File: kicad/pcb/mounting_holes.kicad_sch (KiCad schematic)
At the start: 34 parts

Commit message: schematic fix and plate tolerance fix
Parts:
- removed H11, H13, H14, H15, H16, H17, H18, H19, H20, H21, H22, H23, H24, H25, H26, H27, H28, H30, H31, H32, H33, H34, H35, H36, H37, H38: M2 Hole, MountingHole:MountingHole_2.2mm_M2_DIN965, symbol Mechanical:MountingHole
- added H1 (x4), H2 (x4), H3 (x3), H4 (x3), H5 (x3), H6 (x2), H7 (x2), H8 (x2): M2 Hole, capacitive_sensors:MountingHole_2.2mm_M2, symbol Mechanical:MountingHole
- added H6, H7, H8: M2 Hole, MountingHole:MountingHole_2.2mm_M2, symbol Mechanical:MountingHole
- H1, H2, H3, H4, H5, H6, H7: footprint MountingHole:MountingHole_2.2mm_M2_DIN965 -> capacitive_sensors:MountingHole_2.2mm_M2
- H8: footprint MountingHole:MountingHole_2.2mm_M2_DIN965 -> MountingHole:MountingHole_2.2mm_M2
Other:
- moved on the sheet: H1, H2, H3, H4, H5, H6, H7, H8

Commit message: remove top mounting hole for chiffre+ compatibility
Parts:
- H5: now not fitted
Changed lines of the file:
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@@
   )
   (symbol (lib_id "Mechanical:MountingHole") (at 50.8 55.88 0) (unit 1)
-    (in_bom yes) (on_board yes) (dnp no) (fields_autoplaced)
+    (in_bom yes) (on_board yes) (dnp yes) (fields_autoplaced)
     (property "Reference" "H5" (at 53.34 54.61 0)
       (effects (font (size 1.27 1.27)) (justify left))
@@
   )
   (symbol (lib_id "Mechanical:MountingHole") (at 50.8 71.12 0) (unit 1)
-    (in_bom yes) (on_board yes) (dnp no) (fields_autoplaced)
+    (in_bom yes) (on_board yes) (dnp yes) (fields_autoplaced)
     (property "Reference" "H5" (at 53.34 69.85 0)
       (effects (font (size 1.27 1.27)) (justify left))

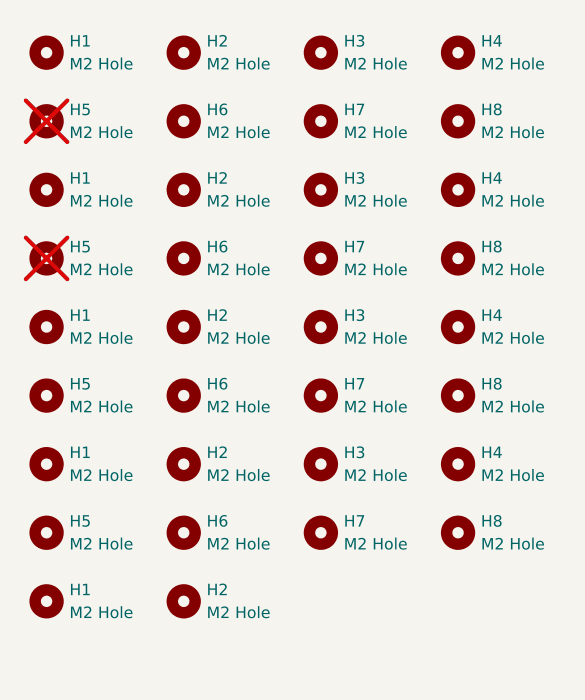
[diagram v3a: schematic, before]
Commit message: Remove extra mounting holes from PCB and update version number.
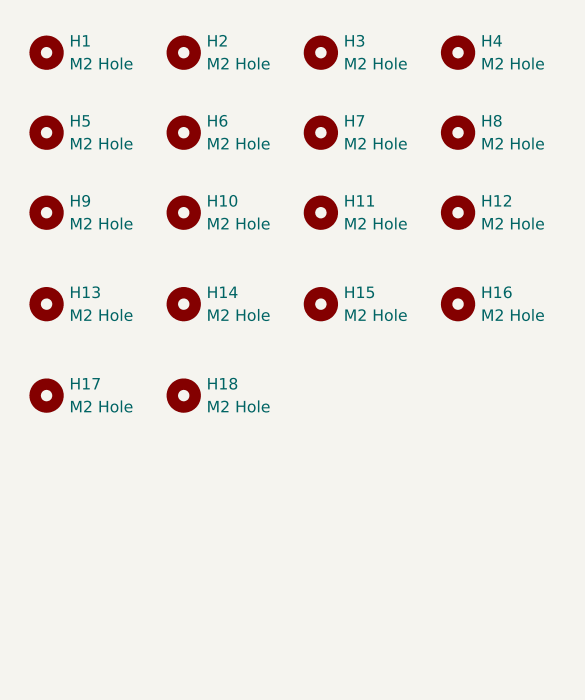
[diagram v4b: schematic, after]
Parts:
- removed H1 (x4), H2 (x4), H3 (x3), H4 (x3), H5 (x4), H6 (x3), H7 (x3), H8 (x2): M2 Hole, capacitive_sensors:MountingHole_2.2mm_M2, symbol Mechanical:MountingHole
- removed H6, H7, H8 (x2): M2 Hole, MountingHole:MountingHole_2.2mm_M2, symbol Mechanical:MountingHole
- added H10, H11, H12, H13, H14, H15, H16, H17, H18, H5, H6, H7, H8, H9: M2 Hole, capacitive_sensors:MountingHole_2.2mm_M2, symbol Mechanical:MountingHole
